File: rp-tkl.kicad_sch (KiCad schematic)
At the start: 33 parts, among them J1 USB_C_Receptacle_USB2.0, J2 SWD, SW0 SW_Push, U1 XC6206PxxxMR, U2 RP2040, U3 SRV05-4, U4 W25Q128JVS, Y1 12MHz

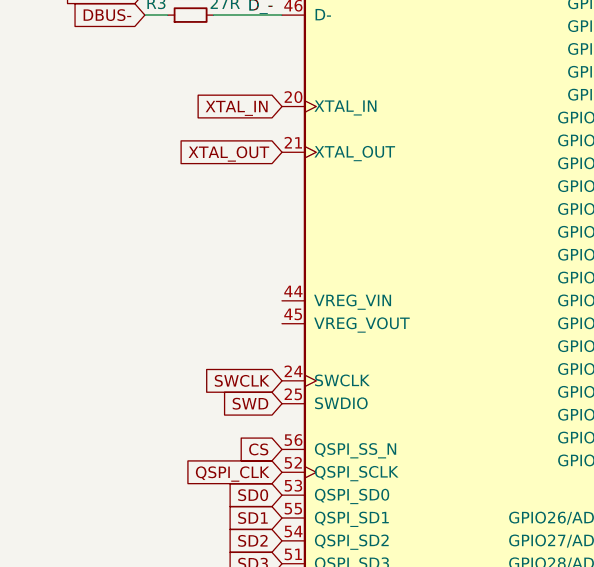
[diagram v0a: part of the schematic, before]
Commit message: [Preliminary] Completed MCU Routing
- Also added some small things that i forgot on schematic
- Need to: connect matrix to mcu
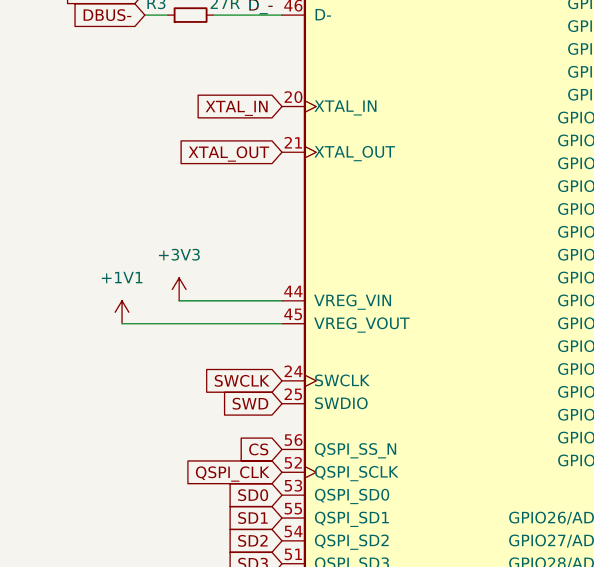
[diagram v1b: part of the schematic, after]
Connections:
- net +1V1: now also U2.45 (VREG_VOUT)
- net +3V3: now also U2.44 (VREG_VIN)
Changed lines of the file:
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@@
+    (stroke (width 0) (type default) (color 0 0 0 0))
+  )
+  (wire (pts (xy 34.29 95.25) (xy 45.72 95.25))
     (stroke (width 0) (type default) (color 0 0 0 0))
   )
@@
   )
   (wire (pts (xy 168.91 118.11) (xy 171.45 118.11))
+    (stroke (width 0) (type default) (color 0 0 0 0))
+  )
+  (wire (pts (xy 45.72 97.79) (xy 27.94 97.79))
     (stroke (width 0) (type default) (color 0 0 0 0))
   )
@@
     (pin "1")
     (pin "2")
+  )
+  (symbol (lib_id "power:+3V3") (at 34.29 95.25 0) (unit 1)
+    (in_bom yes) (on_board yes) (fields_autoplaced)
+    (property "Reference" "#PWR?" (id 0) (at 34.29 99.06 0)
+      (effects (font (size 1.27 1.27)) hide)
+    )
+    (property "Value" "+3V3" (id 1) (at 34.29 90.17 0))
+    (property "Footprint" "" (id 2) (at 34.29 95.25 0)
+      (effects (font (size 1.27 1.27)) hide)
+    )
+    (property "Datasheet" "" (id 3) (at 34.29 95.25 0)
+      (effects (font (size 1.27 1.27)) hide)
+    )
+    (pin "1")
   )
   (symbol (lib_id "power:+3V3") (at 53.34 41.91 0) (unit 1)
@@
     (pin "4")
     (pin "5")
+  )
+  (symbol (lib_id "power:+1V1") (at 27.94 97.79 0) (unit 1)
+    (in_bom yes) (on_board yes)
+    (property "Reference" "#PWR?" (id 0) (at 27.94 101.6 0)
+      (effects (font (size 1.27 1.27)) hide)
+    )
+    (property "Value" "+1V1" (id 1) (at 27.94 92.71 0))
+    (property "Footprint" "" (id 2) (at 27.94 97.79 0)
+      (effects (font (size 1.27 1.27)) hide)
+    )
+    (property "Datasheet" "" (id 3) (at 27.94 97.79 0)
+      (effects (font (size 1.27 1.27)) hide)
+    )
+    (pin "1")
   )
   (symbol (lib_id "power:+3V3") (at 168.91 163.83 0) (unit 1)
@@
       (reference "#PWR027") (unit 1) (value "GND") (footprint "")
     )
+    (path "/13bc3998-5745-424e-ada9-f8a9e1f5329c"
+      (reference "#PWR?") (unit 1) (value "+3V3") (footprint "")
+    )
+    (path "/4ba9e55e-16a7-4d09-ba02-77625474432c"
+      (reference "#PWR?") (unit 1) (value "+1V1") (footprint "")
+    )
     (path "/29f11a32-f398-46d6-95a0-57f3be58392e"
